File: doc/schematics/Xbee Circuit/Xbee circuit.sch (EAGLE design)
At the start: 7 parts

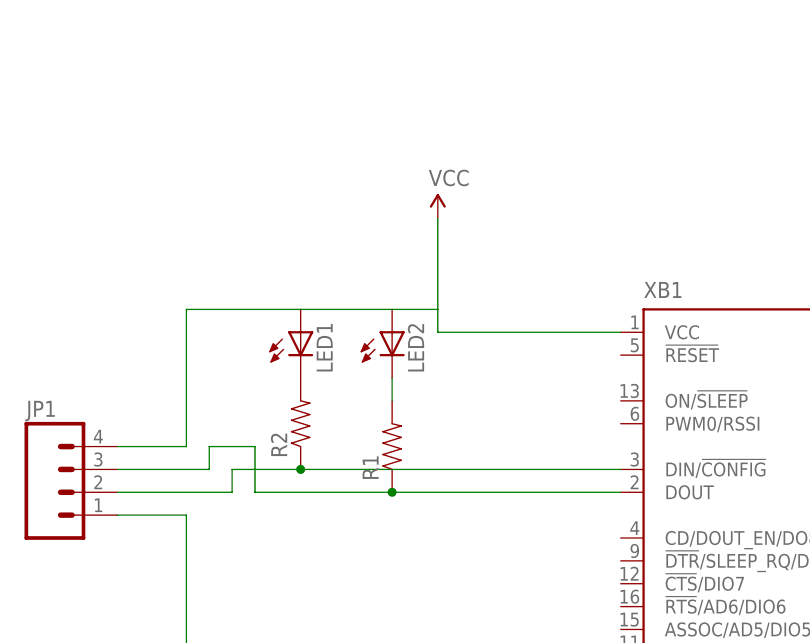
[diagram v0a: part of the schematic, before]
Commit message: New Schematics and Mavlink changes to print f
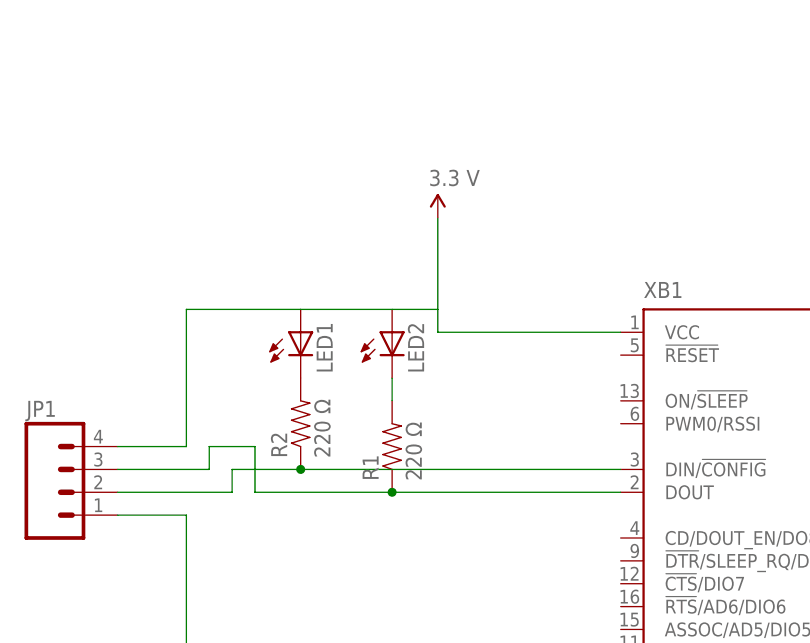
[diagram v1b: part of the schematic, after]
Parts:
- R1, R2: value (none) -> 220 Ω
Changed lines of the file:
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@@
 <grid distance="0.1" unitdist="inch" unit="inch" style="lines" multiple="1" display="no" altdistance="0.01" altunitdist="inch" altunit="inch"/>
 <layers>
-<layer number="1" name="Top" color="4" fill="1" visible="yes" active="no"/>
-<layer number="16" name="Bottom" color="1" fill="1" visible="yes" active="no"/>
-<layer number="17" name="Pads" color="2" fill="1" visible="yes" active="no"/>
-<layer number="18" name="Vias" color="2" fill="1" visible="yes" active="no"/>
-<layer number="19" name="Unrouted" color="6" fill="1" visible="yes" active="no"/>
-<layer number="20" name="Dimension" color="15" fill="1" visible="yes" active="no"/>
-<layer number="21" name="tPlace" color="16" fill="1" visible="yes" active="no"/>
-<layer number="22" name="bPlace" color="14" fill="1" visible="yes" active="no"/>
-<layer number="23" name="tOrigins" color="15" fill="1" visible="yes" active="no"/>
-<layer number="24" name="bOrigins" color="15" fill="1" visible="yes" active="no"/>
-<layer number="25" name="tNames" color="7" fill="1" visible="yes" active="no"/>
-<layer number="26" name="bNames" color="7" fill="1" visible="yes" active="no"/>
-<layer number="27" name="tValues" color="7" fill="1" visible="yes" active="no"/>
-<layer number="28" name="bValues" color="7" fill="1" visible="yes" active="no"/>
+<layer number="1" name="Top" color="4" fill="1" visible="no" active="no"/>
+<layer number="16" name="Bottom" color="1" fill="1" visible="no" active="no"/>
+<layer number="17" name="Pads" color="2" fill="1" visible="no" active="no"/>
+<layer number="18" name="Vias" color="2" fill="1" visible="no" active="no"/>
+<layer number="19" name="Unrouted" color="6" fill="1" visible="no" active="no"/>
+<layer number="20" name="Dimension" color="15" fill="1" visible="no" active="no"/>
+<layer number="21" name="tPlace" color="16" fill="1" visible="no" active="no"/>
+<layer number="22" name="bPlace" color="14" fill="1" visible="no" active="no"/>
+<layer number="23" name="tOrigins" color="15" fill="1" visible="no" active="no"/>
+<layer number="24" name="bOrigins" color="15" fill="1" visible="no" active="no"/>
+<layer number="25" name="tNames" color="7" fill="1" visible="no" active="no"/>
+<layer number="26" name="bNames" color="7" fill="1" visible="no" active="no"/>
+<layer number="27" name="tValues" color="7" fill="1" visible="no" active="no"/>
+<layer number="28" name="bValues" color="7" fill="1" visible="no" active="no"/>
 <layer number="29" name="tStop" color="7" fill="3" visible="no" active="no"/>
 <layer number="30" name="bStop" color="7" fill="6" visible="no" active="no"/>
@@
 <layer number="35" name="tGlue" color="7" fill="4" visible="no" active="no"/>
 <layer number="36" name="bGlue" color="7" fill="5" visible="no" active="no"/>
-<layer number="37" name="tTest" color="7" fill="1" visible="yes" active="no"/>
-<layer number="38" name="bTest" color="7" fill="1" visible="yes" active="no"/>
+<layer number="37" name="tTest" color="7" fill="1" visible="no" active="no"/>
+<layer number="38" name="bTest" color="7" fill="1" visible="no" active="no"/>
 <layer number="39" name="tKeepout" color="4" fill="11" visible="no" active="no"/>
 <layer number="40" name="bKeepout" color="1" fill="11" visible="no" active="no"/>
@@
 <layer number="44" name="Drills" color="7" fill="1" visible="no" active="no"/>
 <layer number="45" name="Holes" color="7" fill="1" visible="no" active="no"/>
-<layer number="46" name="Milling" color="3" fill="1" visible="yes" active="no"/>
-<layer number="47" name="Measures" color="7" fill="1" visible="yes" active="no"/>
-<layer number="48" name="Document" color="7" fill="1" visible="yes" active="no"/>
-<layer number="49" name="Reference" color="7" fill="1" visible="yes" active="no"/>
-<layer number="50" name="dxf" color="7" fill="1" visible="yes" active="no"/>
-<layer number="51" name="tDocu" color="6" fill="1" visible="yes" active="no"/>
-<layer number="52" name="bDocu" color="7" fill="1" visible="yes" active="no"/>
-<layer number="53" name="tGND_GNDA" color="7" fill="9" visible="yes" active="no"/>
-<layer number="54" name="bGND_GNDA" color="1" fill="9" visible="yes" active="no"/>
-<layer number="56" name="wert" color="7" fill="1" visible="yes" active="no"/>
+<layer number="46" name="Milling" color="3" fill="1" visible="no" active="no"/>
+<layer number="47" name="Measures" color="7" fill="1" visible="no" active="no"/>
+<layer number="48" name="Document" color="7" fill="1" visible="no" active="no"/>
+<layer number="49" name="Reference" color="7" fill="1" visible="no" active="no"/>
+<layer number="50" name="dxf" color="7" fill="1" visible="no" active="no"/>
+<layer number="51" name="tDocu" color="6" fill="1" visible="no" active="no"/>
+<layer number="52" name="bDocu" color="7" fill="1" visible="no" active="no"/>
+<layer number="53" name="tGND_GNDA" color="7" fill="9" visible="no" active="no"/>
+<layer number="54" name="bGND_GNDA" color="1" fill="9" visible="no" active="no"/>
+<layer number="56" name="wert" color="7" fill="1" visible="no" active="no"/>
 <layer number="91" name="Nets" color="2" fill="1" visible="yes" active="yes"/>
 <layer number="92" name="Busses" color="1" fill="1" visible="yes" active="yes"/>
@@
 <part name="LED1" library="SparkFun-LED" deviceset="LED" device="5MM"/>
 <part name="LED2" library="SparkFun-LED" deviceset="LED" device="5MM"/>
-<part name="R1" library="SparkFun-Resistors" deviceset="RESISTOR" device="PTH-1/4W"/>
-<part name="R2" library="SparkFun-Resistors" deviceset="RESISTOR" device="PTH-1/4W"/>
-<part name="SUPPLY1" library="SparkFun-Aesthetics" deviceset="VCC" device=""/>
+<part name="R1" library="SparkFun-Resistors" deviceset="RESISTOR" device="PTH-1/4W" value="220 Ω"/>
+<part name="R2" library="SparkFun-Resistors" deviceset="RESISTOR" device="PTH-1/4W" value="220 Ω"/>
+<part name="3.3V" library="SparkFun-Aesthetics" deviceset="VCC" device="" value="3.3 V"/>
 <part name="GND1" library="SparkFun-Aesthetics" deviceset="GND" device=""/>
 <part name="JP1" library="SparkFun-Connectors" deviceset="M04" device="LOCK"/>
@@
 <instance part="R1" gate="G$1" x="58.42" y="116.84" rot="R90"/>
 <instance part="R2" gate="G$1" x="48.26" y="119.38" rot="R90"/>
-<instance part="SUPPLY1" gate="1" x="63.5" y="142.24"/>
+<instance part="3.3V" gate="1" x="63.5" y="142.24"/>
 <instance part="GND1" gate="1" x="60.96" y="73.66"/>
 <instance part="JP1" gate="G$1" x="22.86" y="111.76"/>
@@
 <wire x1="83.82" y1="129.54" x2="63.5" y2="129.54" width="0.1524" layer="91"/>
 <wire x1="63.5" y1="129.54" x2="63.5" y2="132.08" width="0.1524" layer="91"/>
-<pinref part="SUPPLY1" gate="1" pin="VCC"/>
+<pinref part="3.3V" gate="1" pin="VCC"/>
 <pinref part="LED2" gate="G$1" pin="A"/>
 <wire x1="63.5" y1="132.08" x2="63.5" y2="142.24" width="0.1524" layer="91"/>

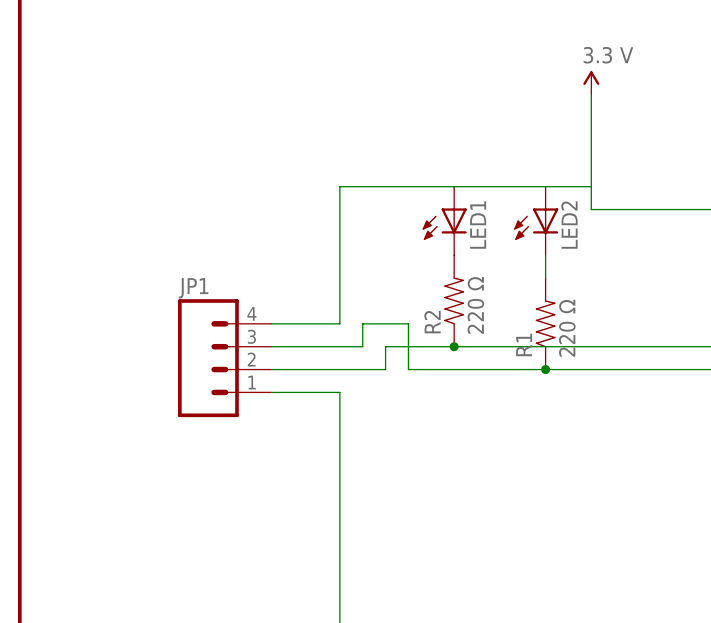
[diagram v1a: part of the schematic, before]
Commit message: Started the barometer message, hit a strange error.
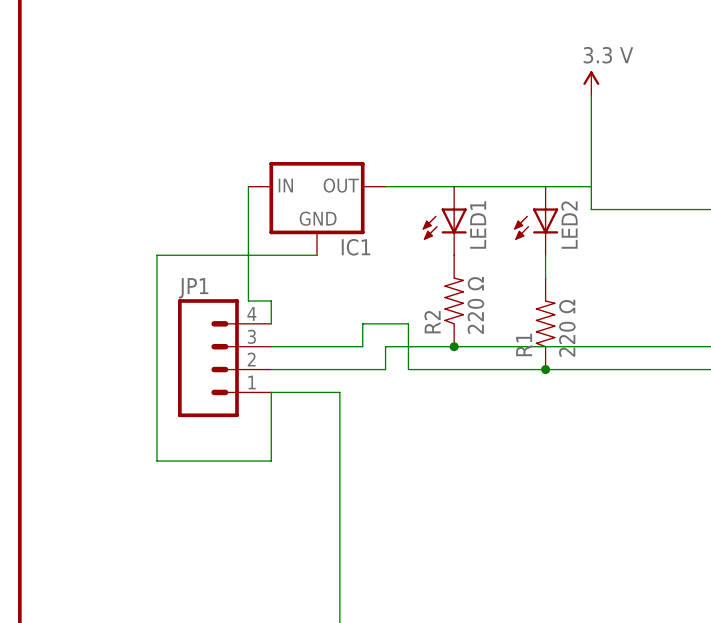
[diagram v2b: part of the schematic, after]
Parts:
- added IC1: (no value), SparkFun-PowerIC:V_REG_78XXSINK
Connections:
- new net N$5: IC1.IN, JP1.4
- net GND: now also IC1.GND
- net VCC: now also IC1.OUT; no longer JP1.4
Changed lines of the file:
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@@
 <layer number="106" name="bPlate" color="7" fill="1" visible="no" active="yes"/>
 <layer number="107" name="Crop" color="7" fill="1" visible="no" active="yes"/>
+<layer number="108" name="tplace-old" color="10" fill="1" visible="yes" active="yes"/>
+<layer number="109" name="ref-old" color="11" fill="1" visible="yes" active="yes"/>
 <layer number="116" name="Patch_BOT" color="9" fill="4" visible="no" active="yes"/>
 <layer number="121" name="_tsilk" color="7" fill="1" visible="no" active="yes"/>
@@
 <part name="JP1" library="SparkFun-Connectors" deviceset="M04" device="LOCK"/>
 <part name="FRAME1" library="SparkFun-Aesthetics" deviceset="FRAME-LETTER" device=""/>
+<part name="IC1" library="SparkFun-PowerIC" deviceset="V_REG_78XX" device="SINK"/>
 </parts>
 <sheets>
@@
 <instance part="FRAME1" gate="G$1" x="0" y="0"/>
 <instance part="FRAME1" gate="G$2" x="147.32" y="0"/>
+<instance part="IC1" gate="G$1" x="33.02" y="132.08"/>
 </instances>
 <busses>
@@
 <pinref part="LED1" gate="G$1" pin="A"/>
 <wire x1="58.42" y1="132.08" x2="48.26" y2="132.08" width="0.1524" layer="91"/>
-<wire x1="35.56" y1="132.08" x2="48.26" y2="132.08" width="0.1524" layer="91"/>
-<wire x1="27.94" y1="116.84" x2="35.56" y2="116.84" width="0.1524" layer="91"/>
-<wire x1="35.56" y1="116.84" x2="35.56" y2="132.08" width="0.1524" layer="91"/>
-<pinref part="JP1" gate="G$1" pin="4"/>
+<pinref part="IC1" gate="G$1" pin="OUT"/>
+<wire x1="48.26" y1="132.08" x2="40.64" y2="132.08" width="0.1524" layer="91"/>
 </segment>
 </net>
@@
 <wire x1="60.96" y1="76.2" x2="83.82" y2="76.2" width="0.1524" layer="91"/>
 <wire x1="35.56" y1="76.2" x2="60.96" y2="76.2" width="0.1524" layer="91"/>
+<pinref part="IC1" gate="G$1" pin="GND"/>
+<wire x1="33.02" y1="124.46" x2="15.24" y2="124.46" width="0.1524" layer="91"/>
+<wire x1="15.24" y1="124.46" x2="15.24" y2="101.6" width="0.1524" layer="91"/>
+<pinref part="JP1" gate="G$1" pin="1"/>
+<wire x1="15.24" y1="101.6" x2="27.94" y2="101.6" width="0.1524" layer="91"/>
+<wire x1="27.94" y1="101.6" x2="27.94" y2="109.22" width="0.1524" layer="91"/>
 <wire x1="27.94" y1="109.22" x2="35.56" y2="109.22" width="0.1524" layer="91"/>
 <wire x1="35.56" y1="109.22" x2="35.56" y2="76.2" width="0.1524" layer="91"/>
-<pinref part="JP1" gate="G$1" pin="1"/>
 </segment>
 </net>
@@
 </segment>
 </net>
+<net name="N$5" class="0">
+<segment>
+<pinref part="IC1" gate="G$1" pin="IN"/>
+<wire x1="25.4" y1="132.08" x2="25.4" y2="119.38" width="0.1524" layer="91"/>
+<pinref part="JP1" gate="G$1" pin="4"/>
+<wire x1="25.4" y1="119.38" x2="27.94" y2="119.38" width="0.1524" layer="91"/>
+<wire x1="27.94" y1="119.38" x2="27.94" y2="116.84" width="0.1524" layer="91"/>
+</segment>
+</net>

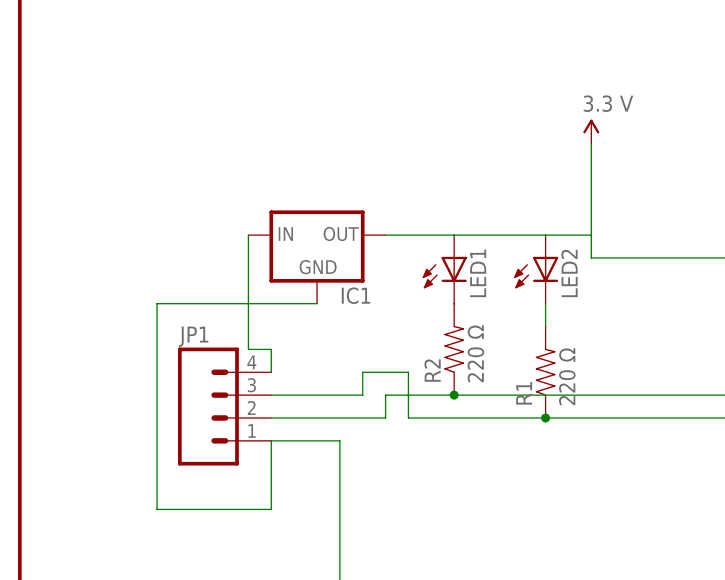
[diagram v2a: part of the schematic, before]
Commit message: Schematics: XBEE finished, Compas Started Power supply: looked at.
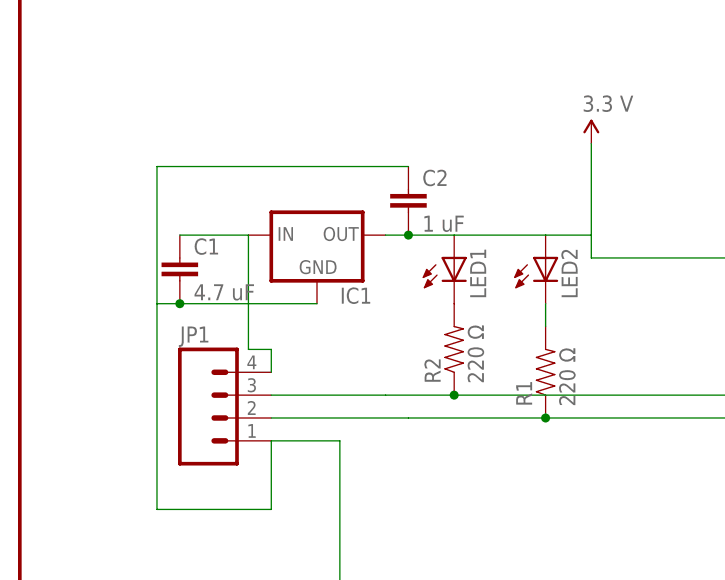
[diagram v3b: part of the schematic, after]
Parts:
- added C1: 4.7 uF, SparkFun-Capacitors:CAP0805
- added C2: 1 uF, SparkFun-Capacitors:CAP0805
- R1, R2: device SparkFun-Resistors:RESISTORPTH-1/4W -> SparkFun-Resistors:RESISTOR0805-RES
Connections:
- net GND: now also C1.2, C2.1
- net N$3: now also JP1.3; no longer JP1.2
- net N$4: now also JP1.2; no longer JP1.3
- net N$5: now also C1.1
- net VCC: now also C2.2
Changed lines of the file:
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@@
 <part name="LED1" library="SparkFun-LED" deviceset="LED" device="5MM"/>
 <part name="LED2" library="SparkFun-LED" deviceset="LED" device="5MM"/>
-<part name="R1" library="SparkFun-Resistors" deviceset="RESISTOR" device="PTH-1/4W" value="220 Ω"/>
-<part name="R2" library="SparkFun-Resistors" deviceset="RESISTOR" device="PTH-1/4W" value="220 Ω"/>
+<part name="R1" library="SparkFun-Resistors" deviceset="RESISTOR" device="0805-RES" value="220 Ω"/>
+<part name="R2" library="SparkFun-Resistors" deviceset="RESISTOR" device="0805-RES" value="220 Ω"/>
 <part name="3.3V" library="SparkFun-Aesthetics" deviceset="VCC" device="" value="3.3 V"/>
 <part name="GND1" library="SparkFun-Aesthetics" deviceset="GND" device=""/>
@@
 <part name="FRAME1" library="SparkFun-Aesthetics" deviceset="FRAME-LETTER" device=""/>
 <part name="IC1" library="SparkFun-PowerIC" deviceset="V_REG_78XX" device="SINK"/>
+<part name="C1" library="SparkFun-Capacitors" deviceset="CAP" device="0805" value="4.7 uF"/>
+<part name="C2" library="SparkFun-Capacitors" deviceset="CAP" device="0805" value="1 uF"/>
 </parts>
 <sheets>
@@
 <instance part="FRAME1" gate="G$2" x="147.32" y="0"/>
 <instance part="IC1" gate="G$1" x="33.02" y="132.08"/>
+<instance part="C1" gate="G$1" x="17.78" y="127"/>
+<instance part="C2" gate="G$1" x="43.18" y="134.62"/>
 </instances>
 <busses>
@@
 <wire x1="58.42" y1="132.08" x2="48.26" y2="132.08" width="0.1524" layer="91"/>
 <pinref part="IC1" gate="G$1" pin="OUT"/>
-<wire x1="48.26" y1="132.08" x2="40.64" y2="132.08" width="0.1524" layer="91"/>
+<wire x1="48.26" y1="132.08" x2="43.18" y2="132.08" width="0.1524" layer="91"/>
+<pinref part="C2" gate="G$1" pin="2"/>
+<wire x1="43.18" y1="132.08" x2="40.64" y2="132.08" width="0.1524" layer="91"/>
+<junction x="43.18" y="132.08"/>
 </segment>
 </net>
@@
 <wire x1="35.56" y1="76.2" x2="60.96" y2="76.2" width="0.1524" layer="91"/>
 <pinref part="IC1" gate="G$1" pin="GND"/>
-<wire x1="33.02" y1="124.46" x2="15.24" y2="124.46" width="0.1524" layer="91"/>
+<wire x1="33.02" y1="124.46" x2="17.78" y2="124.46" width="0.1524" layer="91"/>
+<wire x1="17.78" y1="124.46" x2="15.24" y2="124.46" width="0.1524" layer="91"/>
 <wire x1="15.24" y1="124.46" x2="15.24" y2="101.6" width="0.1524" layer="91"/>
 <pinref part="JP1" gate="G$1" pin="1"/>
@@
 <wire x1="27.94" y1="109.22" x2="35.56" y2="109.22" width="0.1524" layer="91"/>
 <wire x1="35.56" y1="109.22" x2="35.56" y2="76.2" width="0.1524" layer="91"/>
+<pinref part="C2" gate="G$1" pin="1"/>
+<wire x1="43.18" y1="139.7" x2="15.24" y2="139.7" width="0.2032" layer="91"/>
+<wire x1="15.24" y1="139.7" x2="15.24" y2="124.46" width="0.2032" layer="91"/>
+<pinref part="C1" gate="G$1" pin="2"/>
+<junction x="17.78" y="124.46"/>
 </segment>
 </net>
@@
 <wire x1="48.26" y1="114.3" x2="40.64" y2="114.3" width="0.1524" layer="91"/>
 <junction x="48.26" y="114.3"/>
-<wire x1="40.64" y1="114.3" x2="40.64" y2="111.76" width="0.1524" layer="91"/>
-<pinref part="JP1" gate="G$1" pin="2"/>
-<wire x1="40.64" y1="111.76" x2="27.94" y2="111.76" width="0.1524" layer="91"/>
+<pinref part="JP1" gate="G$1" pin="3"/>
+<wire x1="40.64" y1="114.3" x2="27.94" y2="114.3" width="0.2032" layer="91"/>
 </segment>
 </net>
@@
 <wire x1="58.42" y1="111.76" x2="43.18" y2="111.76" width="0.1524" layer="91"/>
 <junction x="58.42" y="111.76"/>
-<wire x1="43.18" y1="111.76" x2="43.18" y2="116.84" width="0.1524" layer="91"/>
-<wire x1="43.18" y1="116.84" x2="38.1" y2="116.84" width="0.1524" layer="91"/>
-<wire x1="38.1" y1="116.84" x2="38.1" y2="114.3" width="0.1524" layer="91"/>
-<pinref part="JP1" gate="G$1" pin="3"/>
-<wire x1="38.1" y1="114.3" x2="27.94" y2="114.3" width="0.1524" layer="91"/>
+<pinref part="JP1" gate="G$1" pin="2"/>
+<wire x1="43.18" y1="111.76" x2="27.94" y2="111.76" width="0.2032" layer="91"/>
 </segment>
 </net>
@@
 <wire x1="25.4" y1="119.38" x2="27.94" y2="119.38" width="0.1524" layer="91"/>
 <wire x1="27.94" y1="119.38" x2="27.94" y2="116.84" width="0.1524" layer="91"/>
+<pinref part="C1" gate="G$1" pin="1"/>
+<wire x1="25.4" y1="132.08" x2="17.78" y2="132.08" width="0.2032" layer="91"/>
 </segment>
 </net>
